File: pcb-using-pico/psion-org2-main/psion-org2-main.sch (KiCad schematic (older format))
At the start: 80 parts, among them J1 Conn_01x24_Female, J2 Conn_01x03_Female, J4 Conn_01x02_Female, J5 Conn_01x02_Female, M1 P-CHANNEL-MOSFET, M2 P-CHANNEL-MOSFET, M3 P-CHANNEL-MOSFET, U1 Pico, U10 AMS1117-3.3, U2 74HC595, U3 Regulator_Switching_MT3608, U4 74LS165, U5 74HC595, U6 AMS1117-5.0, U7 MCP7940N-xSN, Y1 32k768Hz

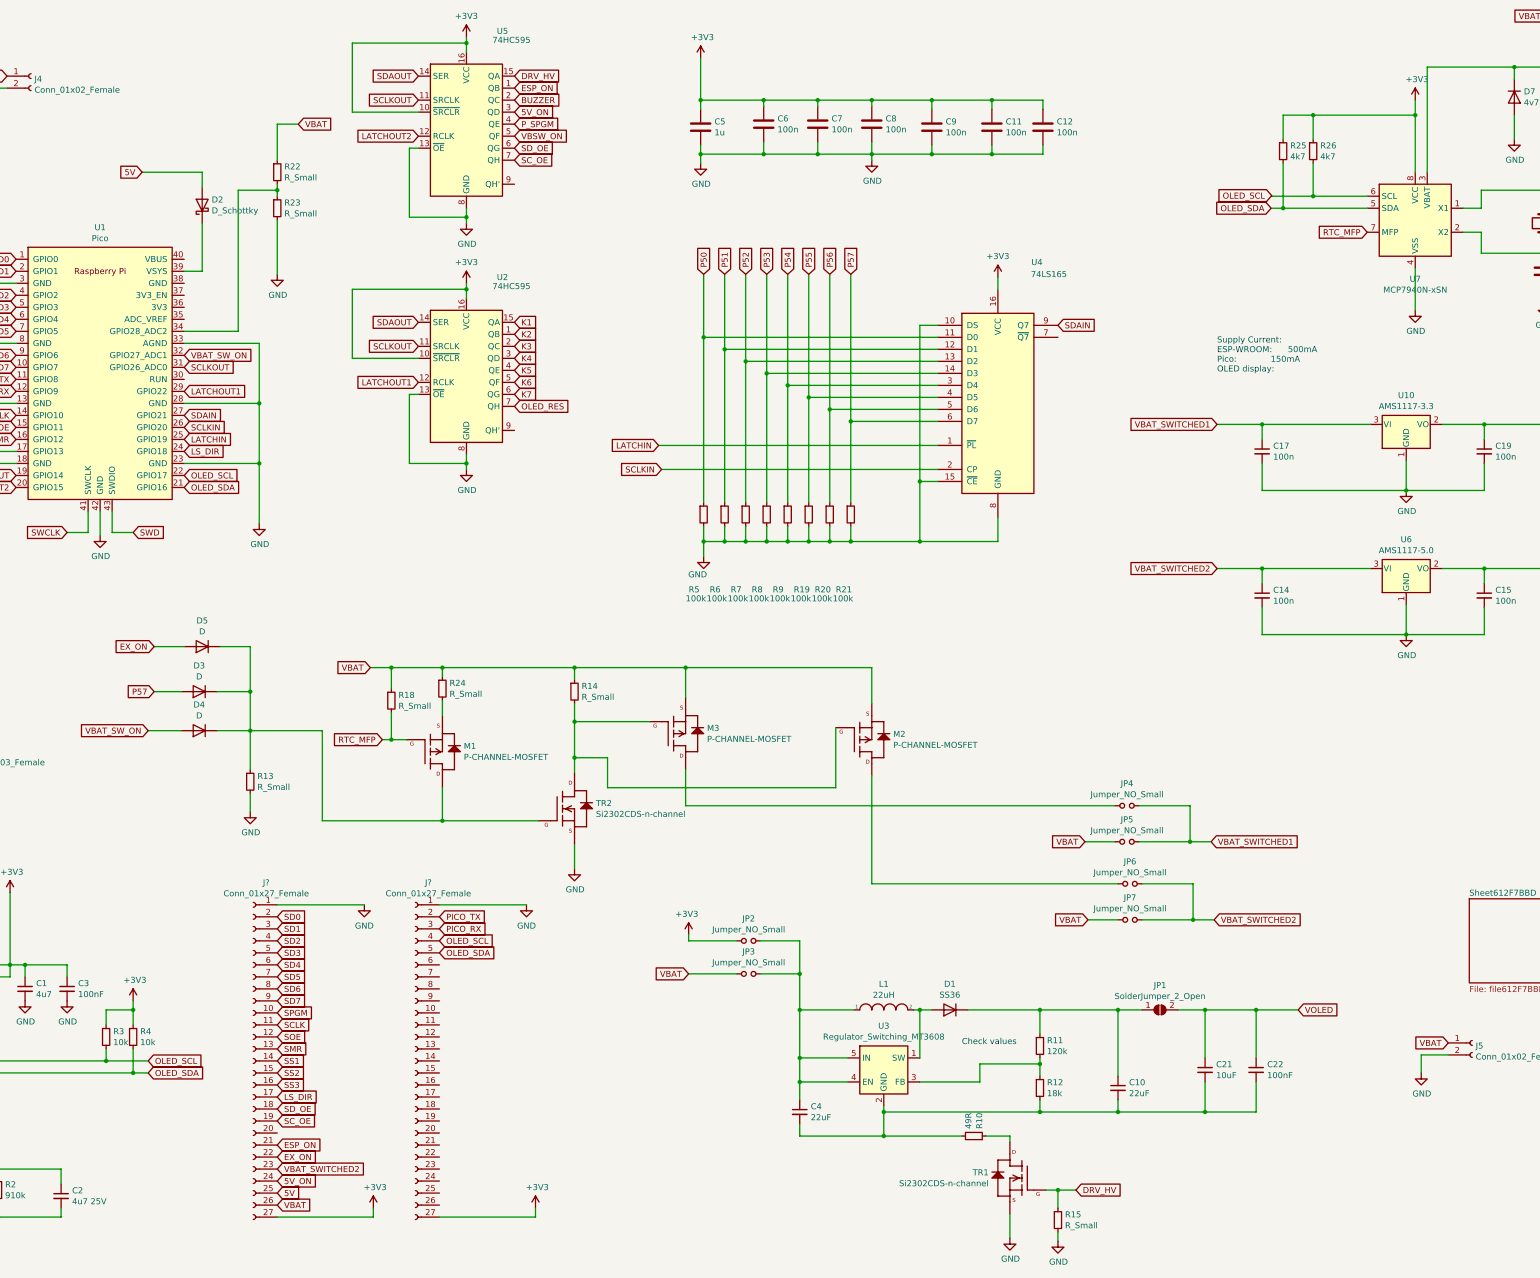
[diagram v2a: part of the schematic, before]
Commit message: Start of PCB layout
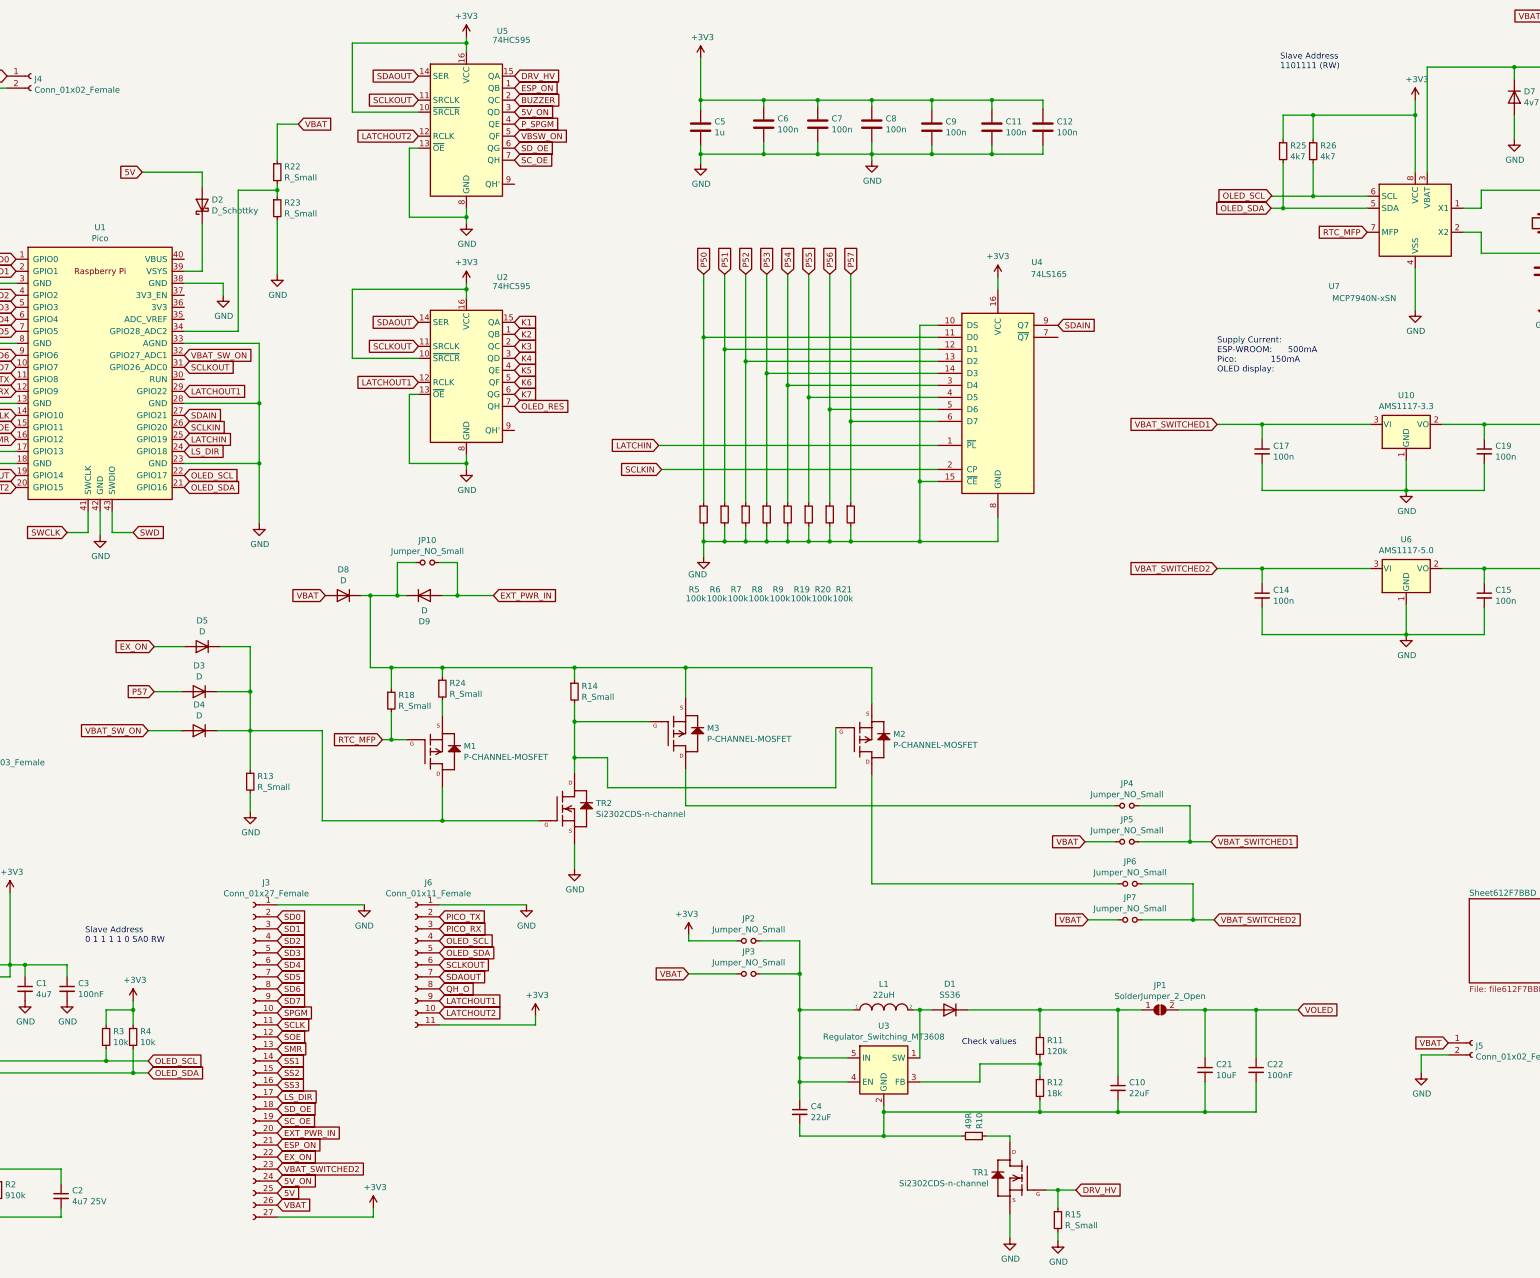
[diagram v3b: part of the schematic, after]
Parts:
- removed J?: Conn_01x27_Female, Connector_PinHeader_2.54mm:PinHeader_1x27_P2.54mm_Vertical, symbol Connector:Conn_01x27_Female
- added D8, D9: D, Diode_SMD:D_SOD-123, symbol Device:D
- added J6: Conn_01x11_Female, Connector_PinHeader_2.54mm:PinHeader_1x11_P2.54mm_Vertical, symbol Connector:Conn_01x11_Female
- added JP10: Jumper_NO_Small, Jumper:SolderJumper-2_P1.3mm_Open_RoundedPad1.0x1.5mm, symbol Device:Jumper_NO_Small
- gave numbers to parts that had none: 1
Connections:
- net +3V3: now also J6.11 (Pin_11)
- net GND: now also U1.38 (GND), J6.1 (Pin_1)
- net LATCHOUT1: now also J6.9 (Pin_9)
- net LATCHOUT2: now also J6.10 (Pin_10)
- net OLED_SCL: now also J6.4 (Pin_4)
- net OLED_SDA: now also J6.5 (Pin_5)
- net PICO_RX: now also J6.3 (Pin_3)
- net PICO_TX: now also J6.2 (Pin_2)
- net SCLKOUT: now also J6.6 (Pin_6)
- net SDAOUT: now also J6.7 (Pin_7)
- net VBAT: now also D8.2 (A); no longer M2.2 (S), M3.2 (S), R14.1, R18.1, R24.1
- net EXT_PWR_IN: now reaches J3.20 (Pin_20)
- net EXT_PWR_IN: now also D9.2 (A), JP10.2
- new net: D8.1 (K), D9.1 (K), JP10.1, M2.2 (S), M3.2 (S), R14.1, R18.1, R24.1
- new net QH_O: J6.8 (Pin_8)
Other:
- note added: "Slave Address\n0 1 1 1 1 0 SA0 RW"
- note added: "Slave Address\n1101111 (RW)"
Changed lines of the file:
@@
 AR Path="/61F3F57A/61F59F4C" Ref="U?"  Part="1"
 AR Path="/61F59F4C" Ref="U7"  Part="1"
-F 0 "U7" H 13825 1861 50  0000 C CNN
-F 1 "MCP7940N-xSN" H 13825 1770 50  0000 C CNN
+F 0 "U7" H 13150 1800 50  0000 C CNN
+F 1 "MCP7940N-xSN" H 13400 1700 50  0000 C CNN
 F 2 "Package_SO:SO-8_3.9x4.9mm_P1.27mm" H 13825 2350 50  0001 C CNN
 F 3 "http://ww1.microchip.com/downloads/en/DeviceDoc/20005010F.pdf" H 13825 2350 50  0001 C CNN
@@
 Text GLabel 3325 6275 0    50   Input ~ 0
 P57
-Text GLabel 5125 6075 0    50   Input ~ 0
+Text GLabel 4750 5475 0    50   Input ~ 0
 VBAT
 Text GLabel 12625 2250 0    50   Input ~ 0
@@
 	4350 8050 5075 8050
 $Comp
-L Connector:Conn_01x27_Female J?
+L Connector:Conn_01x27_Female J3
 U 1 1 6245D35C
 P 4150 9350
-F 0 "J?" H 4042 10835 50  0000 C CNN
+F 0 "J3" H 4042 10835 50  0000 C CNN
 F 1 "Conn_01x27_Female" H 4042 10744 50  0000 C CNN
 F 2 "Connector_PinHeader_2.54mm:PinHeader_1x27_P2.54mm_Vertical" H 4150 9350 50  0001 C CNN
@@
 $EndComp
 $Comp
-L power:+3V3 #PWR?
+L power:+3V3 #PWR0118
 U 1 1 6245D362
 P 5150 10575
-F 0 "#PWR?" H 5150 10425 50  0001 C CNN
+F 0 "#PWR0118" H 5150 10425 50  0001 C CNN
 F 1 "+3V3" H 5165 10748 50  0000 C CNN
 F 2 "" H 5150 10575 50  0001 C CNN
@@
 P 5075 8050
 AR Path="/6104FF77/6245D368" Ref="#PWR?"  Part="1"
-AR Path="/6245D368" Ref="#PWR?"  Part="1"
-F 0 "#PWR?" H 5075 7800 50  0001 C CNN
+AR Path="/6245D368" Ref="#PWR0119"  Part="1"
+F 0 "#PWR0119" H 5075 7800 50  0001 C CNN
 F 1 "GND" H 5075 7875 50  0000 C CNN
 F 2 "" H 5075 8050 50  0001 C CNN
@@
 Text GLabel 4350 8250 2    50   Input ~ 0
 SD1
-$Comp
-L Connector:Conn_01x27_Female J?
-U 1 1 624A5169
-P 5500 9350
-F 0 "J?" H 5392 10835 50  0000 C CNN
-F 1 "Conn_01x27_Female" H 5392 10744 50  0000 C CNN
-F 2 "Connector_PinHeader_2.54mm:PinHeader_1x27_P2.54mm_Vertical" H 5500 9350 50  0001 C CNN
-F 3 "~" H 5500 9350 50  0001 C CNN
-	1    5500 9350
-	-1   0    0    -1
-$EndComp
-Wire Wire Line
-	5700 10650 6500 10650
-Wire Wire Line
-	6500 10650 6500 10575
+Wire Wire Line
+	5700 9050 6500 9050
+Wire Wire Line
+	6500 9050 6500 8975
 Wire Wire Line
 	5700 8050 6425 8050
 $Comp
-L power:+3V3 #PWR?
+L power:+3V3 #PWR0120
 U 1 1 624EB449
-P 6500 10575
-F 0 "#PWR?" H 6500 10425 50  0001 C CNN
-F 1 "+3V3" H 6515 10748 50  0000 C CNN
-F 2 "" H 6500 10575 50  0001 C CNN
-F 3 "" H 6500 10575 50  0001 C CNN
-	1    6500 10575
+P 6500 8975
+F 0 "#PWR0120" H 6500 8825 50  0001 C CNN
+F 1 "+3V3" H 6515 9148 50  0000 C CNN
+F 2 "" H 6500 8975 50  0001 C CNN
+F 3 "" H 6500 8975 50  0001 C CNN
+	1    6500 8975
 	1    0    0    -1
 $EndComp
@@
 P 6425 8050
 AR Path="/6104FF77/624EB44F" Ref="#PWR?"  Part="1"
-AR Path="/624EB44F" Ref="#PWR?"  Part="1"
-F 0 "#PWR?" H 6425 7800 50  0001 C CNN
+AR Path="/624EB44F" Ref="#PWR0121"  Part="1"
+F 0 "#PWR0121" H 6425 7800 50  0001 C CNN
 F 1 "GND" H 6425 7875 50  0000 C CNN
 F 2 "" H 6425 8050 50  0001 C CNN
@@
 Text GLabel 6325 1850 2    50   Input ~ 0
 SC_OE
+Text GLabel 5700 8950 2    50   Input ~ 0
+LATCHOUT2
+Text GLabel 5700 8850 2    50   Input ~ 0
+LATCHOUT1
+Text GLabel 5700 8650 2    50   Input ~ 0
+SDAOUT
+Text GLabel 5700 8550 2    50   Input ~ 0
+SCLKOUT
+Text GLabel 5700 8750 2    50   Input ~ 0
+QH_O
+Text Notes 12700 1100 0    50   ~ 0
+Slave Address\n1101111 (RW)
+Text Notes 2750 8375 0    50   ~ 0
+Slave Address\n0 1 1 1 1 0 SA0 RW
+$Comp
+L Connector:Conn_01x11_Female J6
+U 1 1 62622985
+P 5500 8550
+F 0 "J6" H 5392 9235 50  0000 C CNN
+F 1 "Conn_01x11_Female" H 5392 9144 50  0000 C CNN
+F 2 "Connector_PinHeader_2.54mm:PinHeader_1x11_P2.54mm_Vertical" H 5500 8550 50  0001 C CNN
+F 3 "~" H 5500 8550 50  0001 C CNN
+	1    5500 8550
+	-1   0    0    -1
+$EndComp
+$Comp
+L Device:D D8
+U 1 1 62654BEA
+P 4900 5475
+F 0 "D8" H 4900 5259 50  0000 C CNN
+F 1 "D" H 4900 5350 50  0000 C CNN
+F 2 "Diode_SMD:D_SOD-123" H 4900 5475 50  0001 C CNN
+F 3 "~" H 4900 5475 50  0001 C CNN
+	1    4900 5475
+	-1   0    0    1
+$EndComp
+Wire Wire Line
+	5050 5475 5125 5475
+Wire Wire Line
+	5125 5475 5125 6075
+$Comp
+L Device:D D9
+U 1 1 626BD11F
+P 5575 5475
+F 0 "D9" H 5575 5259 50  0000 C CNN
+F 1 "D" H 5575 5350 50  0000 C CNN
+F 2 "Diode_SMD:D_SOD-123" H 5575 5475 50  0001 C CNN
+F 3 "~" H 5575 5475 50  0001 C CNN
+	1    5575 5475
+	1    0    0    -1
+$EndComp
+Wire Wire Line
+	5425 5475 5350 5475
+Connection ~ 5125 5475
+Text GLabel 6150 5475 2    50   Input ~ 0
+EXT_PWR_IN
+Wire Wire Line
+	5725 5475 5850 5475
+$Comp
+L Device:Jumper_NO_Small JP10
+U 1 1 6274C629
+P 5600 5200
+F 0 "JP10" H 5600 5385 50  0000 C CNN
+F 1 "Jumper_NO_Small" H 5600 5294 50  0000 C CNN
+F 2 "Jumper:SolderJumper-2_P1.3mm_Open_RoundedPad1.0x1.5mm" H 5600 5200 50  0001 C CNN
+F 3 "~" H 5600 5200 50  0001 C CNN
+	1    5600 5200
+	1    0    0    -1
+$EndComp
+Wire Wire Line
+	5700 5200 5850 5200
+Wire Wire Line
+	5850 5200 5850 5475
+Connection ~ 5850 5475
+Wire Wire Line
+	5850 5475 6150 5475
+Wire Wire Line
+	5500 5200 5350 5200
+Wire Wire Line
+	5350 5200 5350 5475
+Connection ~ 5350 5475
+Wire Wire Line
+	5350 5475 5125 5475
+Text GLabel 4350 9950 2    50   Input ~ 0
+EXT_PWR_IN
+$Comp
+L power:GND #PWR?
+U 1 1 627A09AF
+P 3900 2975
+F 0 "#PWR?" H 3900 2725 50  0001 C CNN
+F 1 "GND" H 3905 2802 50  0000 C CNN
+F 2 "" H 3900 2975 50  0001 C CNN
+F 3 "" H 3900 2975 50  0001 C CNN
+	1    3900 2975
+	1    0    0    -1
+$EndComp
+Wire Wire Line
+	3575 2875 3900 2875
+Wire Wire Line
+	3900 2875 3900 2975
 $EndSCHEMATC
